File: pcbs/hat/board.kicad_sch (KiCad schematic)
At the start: 1 part, among them U17 NUCLEO-F401RE

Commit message: cleanup
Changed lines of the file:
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@@
 (kicad_sch (version 20211123) (generator eeschema)
   (paper "A4")
-  (junction (at 170.18 146.05) (diameter 0) (color 0 0 0 0)
+  (junction (at 98.425 19.05) (diameter 0) (color 0 0 0 0)
   )
   (junction (at 101.6 146.05) (diameter 0) (color 0 0 0 0)
@@
     (stroke (width 0) (type default) (color 0 0 0 0))
   )
-  (bus_entry (at 101.6 115.57) (size 2.54 -2.54)
+  (bus_entry (at 98.425 115.57) (size 2.54 -2.54)
     (stroke (width 0) (type default) (color 0 0 0 0))
   )
@@
     (stroke (width 0) (type default) (color 0 0 0 0))
   )
-  (bus_entry (at 101.6 110.49) (size 2.54 -2.54)
+  (bus_entry (at 98.425 110.49) (size 2.54 -2.54)
     (stroke (width 0) (type default) (color 0 0 0 0))
   )
@@
     (stroke (width 0) (type default) (color 0 0 0 0))
   )
-  (bus_entry (at 101.6 107.95) (size 2.54 -2.54)
-    (stroke (width 0) (type default) (color 0 0 0 0))
-  )
-  (bus_entry (at 101.6 113.03) (size 2.54 -2.54)
+  (bus_entry (at 98.425 107.95) (size 2.54 -2.54)
+    (stroke (width 0) (type default) (color 0 0 0 0))
+  )
+  (bus_entry (at 98.425 113.03) (size 2.54 -2.54)
     (stroke (width 0) (type default) (color 0 0 0 0))
   )
@@
     (stroke (width 0) (type default) (color 0 0 0 0))
   )
+  (bus (pts (xy 98.425 19.05) (xy 170.18 19.05))
+    (stroke (width 0) (type default) (color 0 0 0 0))
+  )
+  (bus (pts (xy 98.425 113.03) (xy 98.425 115.57))
+    (stroke (width 0) (type default) (color 0 0 0 0))
+  )
   (wire (pts (xy 27.94 92.71) (xy 44.45 92.71))
     (stroke (width 0) (type default) (color 0 0 0 0))
   )
-  (bus (pts (xy 170.18 69.85) (xy 170.18 146.05))
-    (stroke (width 0) (type default) (color 0 0 0 0))
-  )
   (wire (pts (xy 104.14 69.85) (xy 120.65 69.85))
     (stroke (width 0) (type default) (color 0 0 0 0))
@@
     (stroke (width 0) (type default) (color 0 0 0 0))
   )
-  (bus (pts (xy 101.6 110.49) (xy 101.6 113.03))
+  (bus (pts (xy 101.6 97.79) (xy 101.6 146.05))
+    (stroke (width 0) (type default) (color 0 0 0 0))
+  )
+  (bus (pts (xy 98.425 115.57) (xy 98.425 128.27))
     (stroke (width 0) (type default) (color 0 0 0 0))
   )
@@
     (stroke (width 0) (type default) (color 0 0 0 0))
   )
+  (bus (pts (xy 98.425 107.95) (xy 98.425 110.49))
+    (stroke (width 0) (type default) (color 0 0 0 0))
+  )
   (wire (pts (xy 104.14 62.23) (xy 120.65 62.23))
     (stroke (width 0) (type default) (color 0 0 0 0))
@@
     (stroke (width 0) (type default) (color 0 0 0 0))
   )
+  (bus (pts (xy 170.18 69.85) (xy 170.18 128.27))
+    (stroke (width 0) (type default) (color 0 0 0 0))
+  )
   (bus (pts (xy 101.6 67.31) (xy 101.6 69.85))
     (stroke (width 0) (type default) (color 0 0 0 0))
@@
     (stroke (width 0) (type default) (color 0 0 0 0))
   )
-  (bus (pts (xy 170.18 146.05) (xy 261.62 146.05))
-    (stroke (width 0) (type default) (color 0 0 0 0))
-  )
   (wire (pts (xy 27.94 90.17) (xy 44.45 90.17))
     (stroke (width 0) (type default) (color 0 0 0 0))
   )
-  (bus (pts (xy 101.6 115.57) (xy 101.6 146.05))
-    (stroke (width 0) (type default) (color 0 0 0 0))
-  )
   (wire (pts (xy 118.745 100.33) (xy 120.65 100.33))
     (stroke (width 0) (type default) (color 0 0 0 0))
   )
-  (wire (pts (xy 104.14 107.95) (xy 120.65 107.95))
+  (wire (pts (xy 100.965 107.95) (xy 120.65 107.95))
     (stroke (width 0) (type default) (color 0 0 0 0))
   )
@@
     (stroke (width 0) (type default) (color 0 0 0 0))
   )
-  (bus (pts (xy 101.6 107.95) (xy 101.6 110.49))
-    (stroke (width 0) (type default) (color 0 0 0 0))
-  )
   (wire (pts (xy 104.14 67.31) (xy 120.65 67.31))
     (stroke (width 0) (type default) (color 0 0 0 0))
@@
     (stroke (width 0) (type default) (color 0 0 0 0))
   )
-  (bus (pts (xy 101.6 113.03) (xy 101.6 115.57))
-    (stroke (width 0) (type default) (color 0 0 0 0))
-  )
   (wire (pts (xy 27.94 110.49) (xy 44.45 110.49))
     (stroke (width 0) (type default) (color 0 0 0 0))
@@
     (stroke (width 0) (type default) (color 0 0 0 0))
   )
-  (bus (pts (xy 31.75 19.05) (xy 266.7 19.05))
+  (bus (pts (xy 98.425 19.05) (xy 98.425 107.95))
+    (stroke (width 0) (type default) (color 0 0 0 0))
+  )
+  (bus (pts (xy 31.75 19.05) (xy 98.425 19.05))
+    (stroke (width 0) (type default) (color 0 0 0 0))
+  )
+  (bus (pts (xy 98.425 110.49) (xy 98.425 113.03))
     (stroke (width 0) (type default) (color 0 0 0 0))
   )
@@
     (stroke (width 0) (type default) (color 0 0 0 0))
   )
-  (bus (pts (xy 170.18 43.815) (xy 170.18 62.23))
+  (bus (pts (xy 170.18 19.05) (xy 170.18 62.23))
     (stroke (width 0) (type default) (color 0 0 0 0))
   )
@@
     (stroke (width 0) (type default) (color 0 0 0 0))
   )
-  (wire (pts (xy 104.14 105.41) (xy 120.65 105.41))
+  (wire (pts (xy 100.965 105.41) (xy 120.65 105.41))
     (stroke (width 0) (type default) (color 0 0 0 0))
   )
@@
     (stroke (width 0) (type default) (color 0 0 0 0))
   )
-  (bus (pts (xy 101.6 146.05) (xy 170.18 146.05))
-    (stroke (width 0) (type default) (color 0 0 0 0))
-  )
-  (bus (pts (xy 101.6 97.79) (xy 101.6 107.95))
+  (bus (pts (xy 101.6 146.05) (xy 261.62 146.05))
     (stroke (width 0) (type default) (color 0 0 0 0))
   )
@@
     (stroke (width 0) (type default) (color 0 0 0 0))
   )
-  (wire (pts (xy 104.14 110.49) (xy 120.65 110.49))
+  (wire (pts (xy 167.64 67.31) (xy 151.13 67.31))
+    (stroke (width 0) (type default) (color 0 0 0 0))
+  )
+  (wire (pts (xy 100.965 110.49) (xy 120.65 110.49))
     (stroke (width 0) (type default) (color 0 0 0 0))
   )
@@
     (stroke (width 0) (type default) (color 0 0 0 0))
   )
-  (wire (pts (xy 104.14 113.03) (xy 120.65 113.03))
+  (wire (pts (xy 100.965 113.03) (xy 120.65 113.03))
     (stroke (width 0) (type default) (color 0 0 0 0))
   )
@@
     (stroke (width 0) (type default) (color 0 0 0 0))
   )
-  (wire (pts (xy 167.64 67.31) (xy 151.13 67.31))
-    (stroke (width 0) (type default) (color 0 0 0 0))
-  )

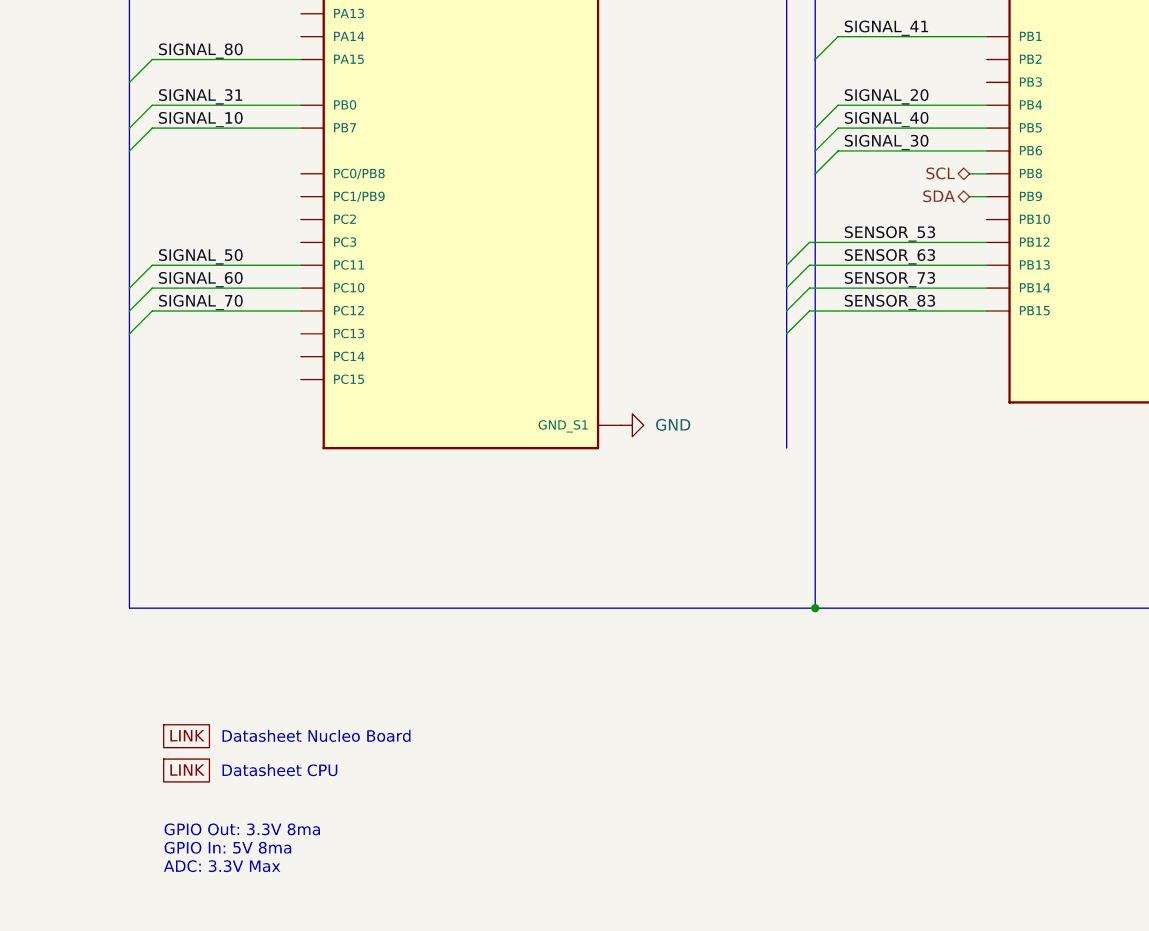
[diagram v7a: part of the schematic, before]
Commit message: add memory + check footprints
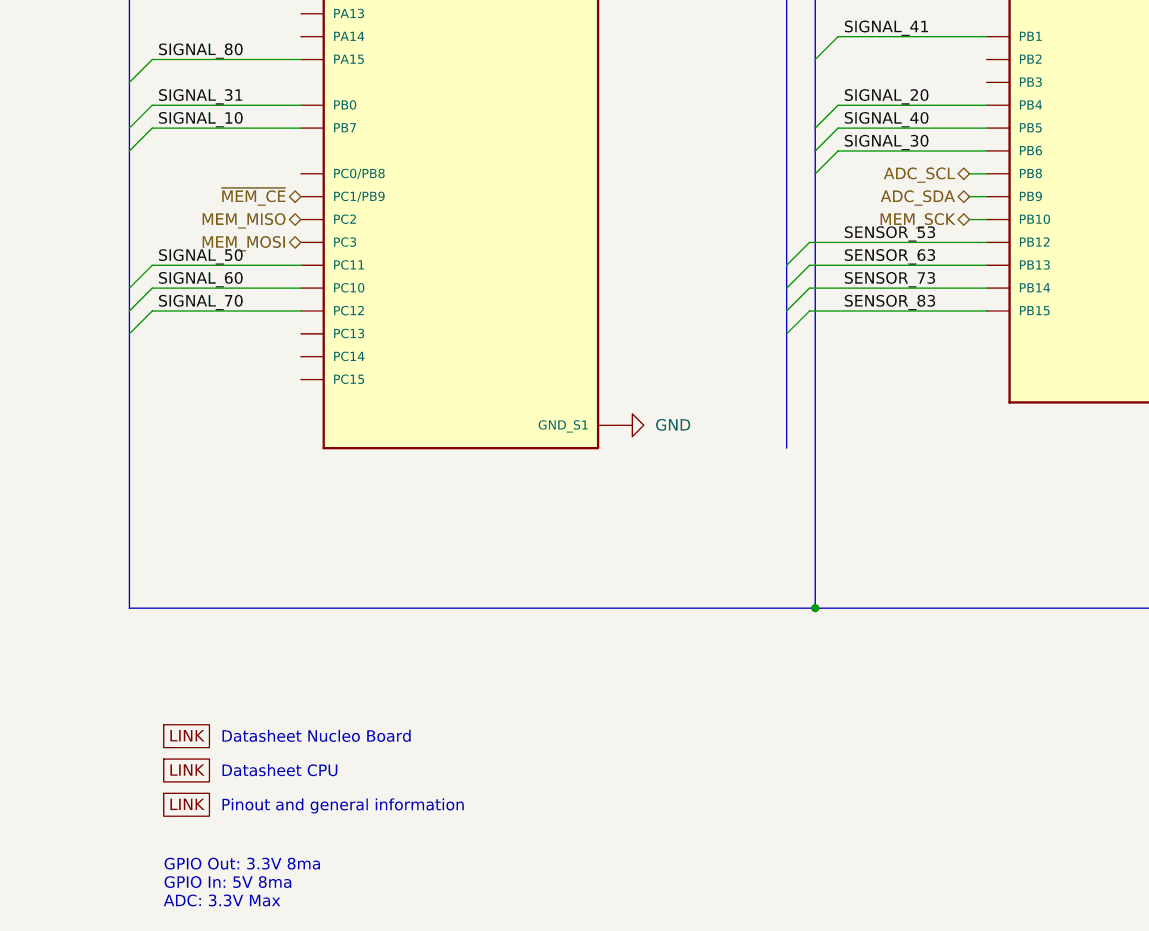
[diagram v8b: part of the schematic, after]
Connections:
- net MEM_MISO: now reaches U17.CN7_35 (PC2)
- net ~{MEM_CE}: now reaches U17.CN7_36 (PC1/PB9)
- net MEM_MOSI: now reaches U17.CN7_37 (PC3)
- net MEM_SCK: now reaches U17.CN10_25 (PB10)
- net SCL renamed ADC_SCL
- net SDA renamed ADC_SDA
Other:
- note added: "Pinout and general information"
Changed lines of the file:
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@@
+    (stroke (width 0) (type default) (color 0 0 0 0))
+  )
+  (wire (pts (xy 118.745 102.87) (xy 120.65 102.87))
     (stroke (width 0) (type default) (color 0 0 0 0))
   )
@@
     (effects (font (size 1.27 1.27)) (justify left bottom))
   )
+  (text "Pinout and general information" (at 35.56 168.91 0)
+    (effects (font (size 1.27 1.27)) (justify left bottom))
+  )
   (text "GPIO Out: 3.3V 8ma\nGPIO In: 5V 8ma\nADC: 3.3V Max\n\n"
-    (at 29.21 177.8 0)
+    (at 29.21 181.61 0)
     (effects (font (size 1.27 1.27)) (justify left bottom))
   )
@@
     (effects (font (size 1.27 1.27)) (justify right bottom))
   )
+  (hierarchical_label "~{MEM_CE}" (shape bidirectional) (at 44.45 100.33 180)
+    (effects (font (size 1.27 1.27)) (justify right))
+  )
   (hierarchical_label "SENSOR_[0..99]" (shape input) (at 31.75 19.05 180)
     (effects (font (size 1.27 1.27)) (justify right))
   )
-  (hierarchical_label "SCL" (shape bidirectional) (at 118.745 97.79 180)
+  (hierarchical_label "ADC_SCL" (shape bidirectional) (at 118.745 97.79 180)
+    (effects (font (size 1.27 1.27)) (justify right))
+  )
+  (hierarchical_label "MEM_SCK" (shape bidirectional) (at 118.745 102.87 180)
+    (effects (font (size 1.27 1.27)) (justify right))
+  )
+  (hierarchical_label "MEM_MOSI" (shape bidirectional) (at 44.45 105.41 180)
+    (effects (font (size 1.27 1.27)) (justify right))
+  )
+  (hierarchical_label "MEM_MISO" (shape bidirectional) (at 44.45 102.87 180)
     (effects (font (size 1.27 1.27)) (justify right))
   )
@@
     (effects (font (size 1.27 1.27)) (justify left))
   )
-  (hierarchical_label "SDA" (shape bidirectional) (at 118.745 100.33 180)
+  (hierarchical_label "ADC_SDA" (shape bidirectional) (at 118.745 100.33 180)
     (effects (font (size 1.27 1.27)) (justify right))
   )
@@
   (symbol (lib_id "STS_Other:Link") (at 31.75 161.29 0) (unit 1)
     (in_bom yes) (on_board yes) (fields_autoplaced)
-    (property "Reference" "#Z17" (id 0) (at 31.75 157.734 0)
+    (property "Reference" "#Z25" (id 0) (at 31.75 157.734 0)
       (effects (font (size 1.27 1.27)) hide)
     )
@@
   (symbol (lib_id "STS_Other:Link") (at 31.75 165.1 0) (unit 1)
     (in_bom yes) (on_board yes) (fields_autoplaced)
-    (property "Reference" "#Z18" (id 0) (at 31.75 161.544 0)
+    (property "Reference" "#Z26" (id 0) (at 31.75 161.544 0)
       (effects (font (size 1.27 1.27)) hide)
     )
@@
       (effects (font (size 1.27 1.27)) hide)
     )
+  )
+  (symbol (lib_id "STS_Other:Link") (at 31.75 168.91 0) (unit 1)
+    (in_bom yes) (on_board yes) (fields_autoplaced)
+    (property "Reference" "#Z27" (id 0) (at 31.75 165.354 0)
+      (effects (font (size 1.27 1.27)) hide)
+    )
+    (property "Value" "Link" (id 1) (at 33.02 165.354 0)
+      (effects (font (size 1.27 1.27)) (justify right) hide)
+    )
+    (property "Footprint" "" (id 2) (at 29.21 166.624 0)
+      (effects (font (size 1.27 1.27)) hide)
+    )
+    (property "Datasheet" "https://os.mbed.com/platforms/ST-Nucleo-F411RE/" (id 3) (at 29.21 166.624 0)
+      (effects (font (size 1.27 1.27)) hide)
+    )
